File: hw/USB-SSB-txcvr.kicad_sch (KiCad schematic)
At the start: 0 parts

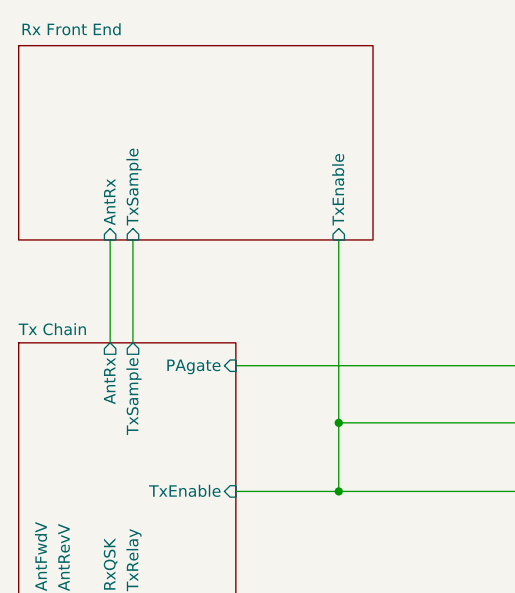
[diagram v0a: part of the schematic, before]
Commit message: Starting to move to 200 ohm share domain with tx and rx with better cheaper faster switching for attenuators and maybe QSK
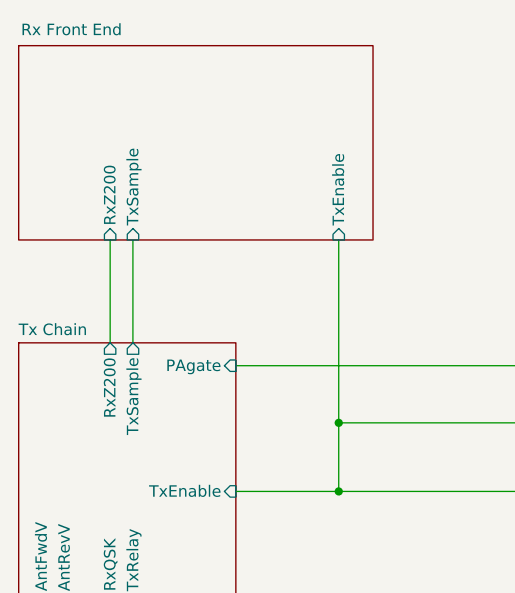
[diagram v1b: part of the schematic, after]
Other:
- sheet Rx Front End ports: added RxZ200; removed AntRx
- sheet Tx Chain ports: added RxZ200; removed AntRx
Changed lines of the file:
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@@
 			)
 		)
-		(pin "AntRx" input
+		(pin "RxZ200" input
 			(at 87.63 64.77 270)
 			(effects
@@
 			)
 		)
-		(pin "AntRx" output
+		(pin "RxZ200" output
 			(at 87.63 76.2 90)
 			(effects

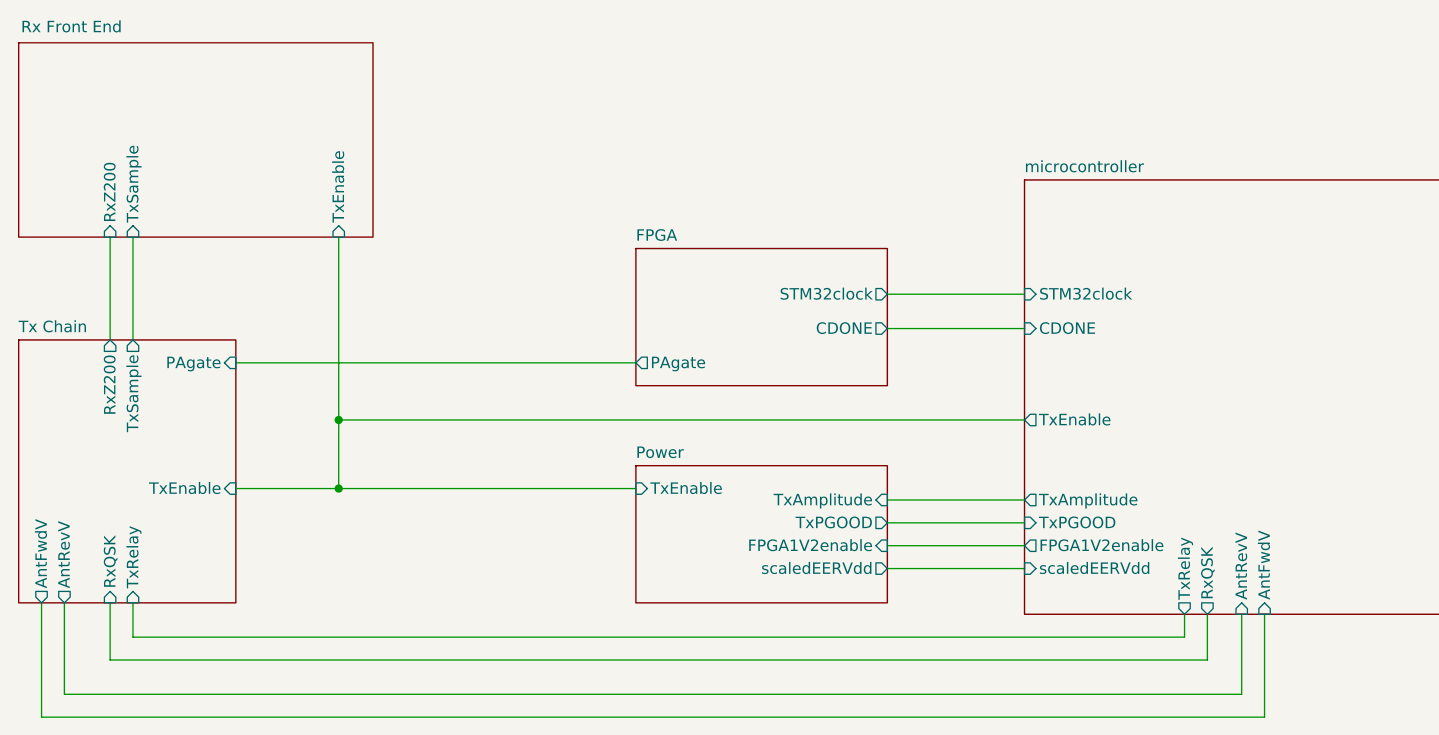
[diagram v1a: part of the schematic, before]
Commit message: Tx Veer changed to 60V max and reviewed. STM32 now provides Bruene sampling signal to control muxes for QSDs0/1 for fwd/rev complex impedance for tuner and VSWR calculation. Preselector now uses pHEMT switches, as does digital attenuator pad in rx path. Tx/rx relay is now in 200 ohm domain and rx shares most of that with tx for good selectivity and to get benefit of antenna tuner.
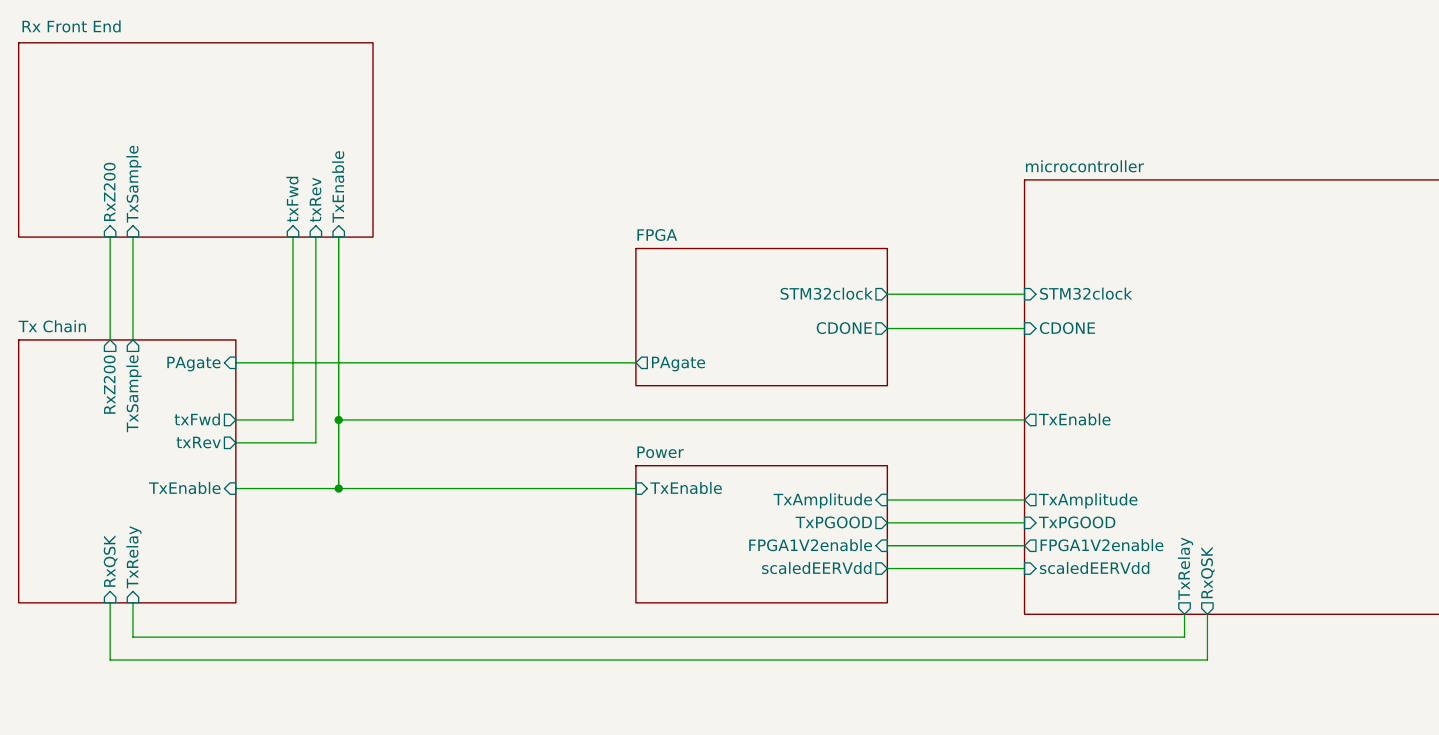
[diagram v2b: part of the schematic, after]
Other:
- sheet Rx Front End ports: added txFwd, txRev; removed none
- sheet Tx Chain ports: added txFwd, txRev; removed AntFwdV, AntRevV
- sheet microcontroller ports: added none; removed AntFwdV, AntRevV
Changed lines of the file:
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@@
 			"qsdSCK" "qsdMOSI" "tuneSCK" "tuneNSS" "tuneMOSI" "tuneMISO" "enable5V"
 			"tmpSCL" "tmpSDA" "qsdPh0a" "qsdPh0b" "qsdPh0c" "qsdPh0d" "qsdPh1a" "qsdPh1b"
-			"qsdPh1c" "qsdPh1d" "qsdPh2a" "qsdPh2b" "qsdPh2c" "qsdPh2d"
+			"qsdPh1c" "qsdPh1d" "qsdPh2a" "qsdPh2b" "qsdPh2c" "qsdPh2d" "bruene"
 		)
 	)
@@
 	(wire
 		(pts
+			(xy 110.49 87.63) (xy 101.6 87.63)
+		)
+		(stroke
+			(width 0)
+			(type default)
+		)
+	)
+	(wire
+		(pts
 			(xy 101.6 92.71) (xy 113.03 92.71)
 		)
@@
 	(wire
 		(pts
-			(xy 80.01 118.11) (xy 215.9 118.11)
-		)
-		(stroke
-			(width 0)
-			(type default)
-		)
-	)
-	(wire
-		(pts
-			(xy 80.01 105.41) (xy 80.01 118.11)
+			(xy 107.95 85.09) (xy 107.95 64.77)
 		)
 		(stroke
@@
 	(wire
 		(pts
-			(xy 82.55 115.57) (xy 82.55 105.41)
-		)
-		(stroke
-			(width 0)
-			(type default)
-		)
-	)
-	(wire
-		(pts
-			(xy 213.36 106.68) (xy 213.36 115.57)
-		)
-		(stroke
-			(width 0)
-			(type default)
-		)
-	)
-	(wire
-		(pts
 			(xy 113.03 64.77) (xy 113.03 85.09)
 		)
@@
 	(wire
 		(pts
-			(xy 213.36 115.57) (xy 82.55 115.57)
+			(xy 110.49 64.77) (xy 110.49 87.63)
 		)
 		(stroke
@@
 	(wire
 		(pts
-			(xy 215.9 118.11) (xy 215.9 106.68)
-		)
-		(stroke
-			(width 0)
-			(type default)
-		)
-	)
-	(wire
-		(pts
 			(xy 207.01 109.22) (xy 90.17 109.22)
 		)
@@
 		(pts
 			(xy 87.63 111.76) (xy 209.55 111.76)
+		)
+		(stroke
+			(width 0)
+			(type default)
+		)
+	)
+	(wire
+		(pts
+			(xy 101.6 85.09) (xy 107.95 85.09)
 		)
 		(stroke
@@
 		(pin "RxZ200" input
 			(at 87.63 64.77 270)
+			(effects
+				(font
+					(size 1.27 1.27)
+				)
+				(justify left)
+			)
+		)
+		(pin "txFwd" input
+			(at 107.95 64.77 270)
+			(effects
+				(font
+					(size 1.27 1.27)
+				)
+				(justify left)
+			)
+		)
+		(pin "txRev" input
+			(at 110.49 64.77 270)
 			(effects
 				(font
@@
 			)
 		)
-		(pin "AntFwdV" output
-			(at 80.01 105.41 270)
-			(effects
-				(font
-					(size 1.27 1.27)
-				)
-				(justify left)
-			)
-		)
-		(pin "AntRevV" output
-			(at 82.55 105.41 270)
-			(effects
-				(font
-					(size 1.27 1.27)
-				)
-				(justify left)
-			)
-		)
 		(pin "RxZ200" output
 			(at 87.63 76.2 90)
@@
 				)
 				(justify left)
+			)
+		)
+		(pin "txFwd" output
+			(at 101.6 85.09 0)
+			(effects
+				(font
+					(size 1.27 1.27)
+				)
+				(justify right)
+			)
+		)
+		(pin "txRev" output
+			(at 101.6 87.63 0)
+			(effects
+				(font
+					(size 1.27 1.27)
+				)
+				(justify right)
 			)
 		)
@@
 			(effects
 				(font
-					(size 1.27 1.27)
-				)
-				(justify left)
-			)
-		)
-		(pin "AntFwdV" input
-			(at 215.9 106.68 270)
-			(effects
-				(font
-					(size 1.27 1.27)
-				)
-				(justify left)
-			)
-		)
-		(pin "AntRevV" input
-			(at 213.36 106.68 270)
-			(effects
-				(font

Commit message: Ready for first schematic review with Claude.ai
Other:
- title: Top Level -> NexRig
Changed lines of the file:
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@@
 	(paper "USLetter")
 	(title_block
-		(title "Top Level")
+		(title "NexRig")
 		(date "2025-08-10")
 		(company "WB7NAB")
@@
 	(bus_alias "Ctrl"
 		(members "audioReset" "qsdBCLK" "qsdMCLK" "qsdWCLK" "qsdData" "qsdNSS"
-			"qsdSCK" "qsdMOSI" "tuneSCK" "tuneNSS" "tuneMOSI" "tuneMISO" "enable5V"
-			"tmpSCL" "tmpSDA" "qsdPh0a" "qsdPh0b" "qsdPh0c" "qsdPh0d" "qsdPh1a" "qsdPh1b"
-			"qsdPh1c" "qsdPh1d" "qsdPh2a" "qsdPh2b" "qsdPh2c" "qsdPh2d" "bruene" "txData"
-			"txBCLK" "txMCLK" "txWCLK" "usbReset" "usbPOK2" "usbPOK3" "usbnALERT"
-			"enable6V" "enFPGASPIVdd" "enFPGAVpp"
+			"qsdSCK" "qsdMOSI" "switchSCK" "switchMOSI" "switchRCK" "enable5V" "tmpSCL"
+			"tmpSDA" "qsdPh0a" "qsdPh0b" "qsdPh0c" "qsdPh0d" "qsdPh1a" "qsdPh1b" "qsdPh1c"
+			"qsdPh1d" "qsdPh2a" "qsdPh2b" "qsdPh2c" "qsdPh2d" "bruene" "txData" "txBCLK"
+			"txMCLK" "txWCLK" "usbReset" "usbPOK2" "usbPOK3" "usbnALERT" "enable6V"
+			"enFPGASPIVdd" "enFPGAVpp"
 		)
 	)

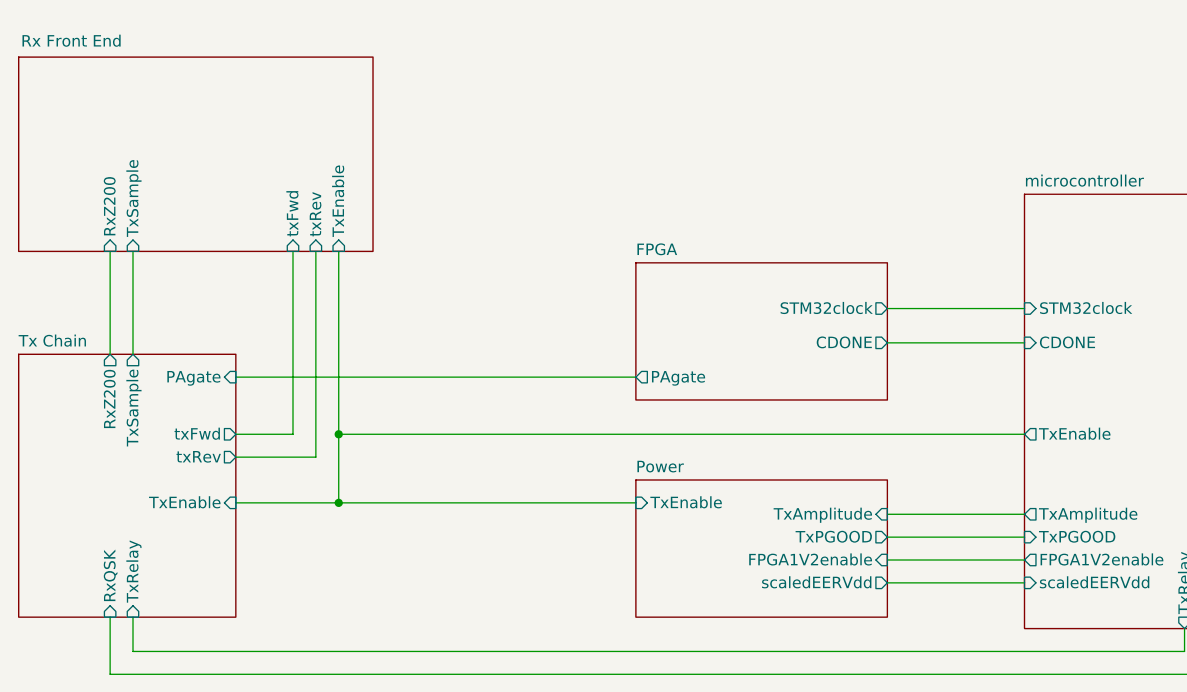
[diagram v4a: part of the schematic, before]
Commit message: Now using H bridge for differential QSE based I/Q tx
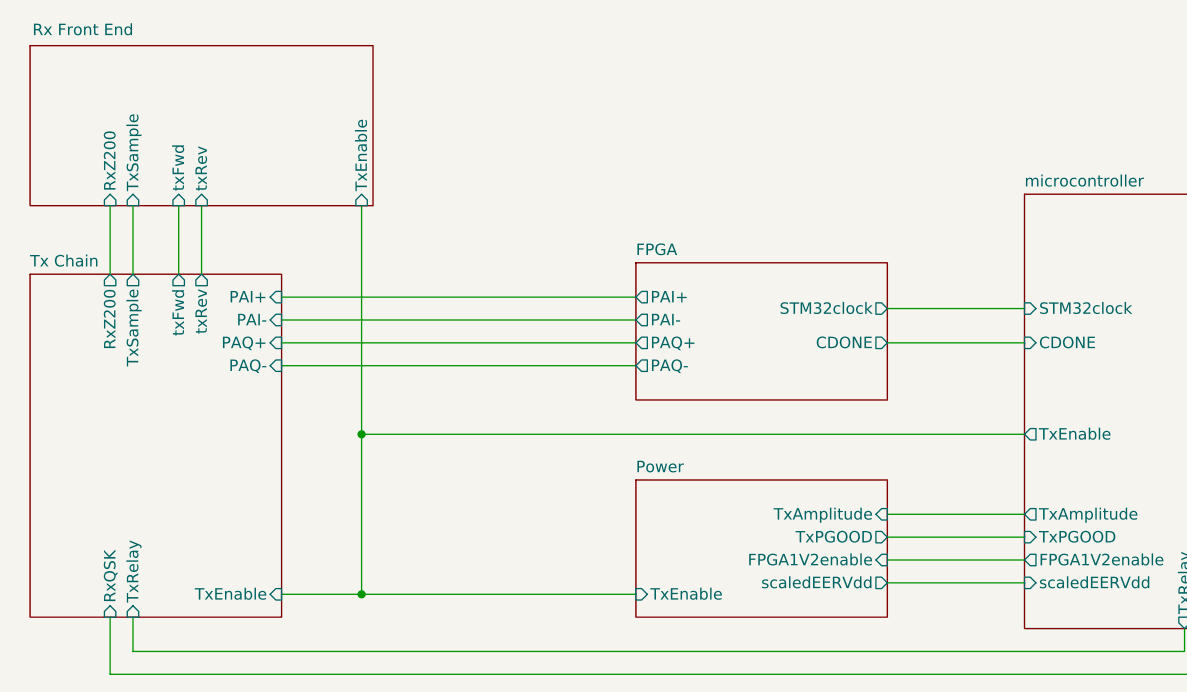
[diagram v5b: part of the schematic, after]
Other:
- sheet FPGA ports: added PAI+, PAI-, PAQ+, PAQ-; removed PAgate
- sheet Tx Chain ports: added PAI+, PAI-, PAQ+, PAQ-; removed PAgate
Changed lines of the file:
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@@
 	)
 	(junction
-		(at 113.03 92.71)
+		(at 115.57 102.87)
 		(diameter 0)
 		(color 0 0 0 0)
 	)
 	(junction
-		(at 113.03 85.09)
+		(at 115.57 85.09)
 		(diameter 0)
 		(color 0 0 0 0)
@@
 	(wire
 		(pts
+			(xy 106.68 72.39) (xy 146.05 72.39)
+		)
+		(stroke
+			(width 0)
+			(type default)
+		)
+	)
+	(wire
+		(pts
 			(xy 87.63 105.41) (xy 87.63 111.76)
 		)
@@
 	(wire
 		(pts
-			(xy 110.49 87.63) (xy 101.6 87.63)
-		)
-		(stroke
-			(width 0)
-			(type default)
-		)
-	)
-	(wire
-		(pts
-			(xy 101.6 92.71) (xy 113.03 92.71)
-		)
-		(stroke
-			(width 0)
-			(type default)
-		)
-	)
-	(wire
-		(pts
-			(xy 113.03 85.09) (xy 113.03 92.71)
-		)
-		(stroke
-			(width 0)
-			(type default)
-		)
-	)
-	(wire
-		(pts
-			(xy 113.03 85.09) (xy 189.23 85.09)
+			(xy 115.57 85.09) (xy 115.57 102.87)
+		)
+		(stroke
+			(width 0)
+			(type default)
+		)
+	)
+	(wire
+		(pts
+			(xy 106.68 102.87) (xy 115.57 102.87)
 		)
 		(stroke
@@
 	(wire
 		(pts
-			(xy 107.95 85.09) (xy 107.95 64.77)
-		)
-		(stroke
-			(width 0)
-			(type default)
-		)
-	)
-	(wire
-		(pts
-			(xy 87.63 64.77) (xy 87.63 76.2)
-		)
-		(stroke
-			(width 0)
-			(type default)
-		)
-	)
-	(wire
-		(pts
-			(xy 113.03 64.77) (xy 113.03 85.09)
+			(xy 115.57 102.87) (xy 146.05 102.87)
+		)
+		(stroke
+			(width 0)
+			(type default)
+		)
+	)
+	(wire
+		(pts
+			(xy 115.57 59.69) (xy 115.57 85.09)
+		)
+		(stroke
+			(width 0)
+			(type default)
+		)
+	)
+	(wire
+		(pts
+			(xy 106.68 69.85) (xy 146.05 69.85)
+		)
+		(stroke
+			(width 0)
+			(type default)
+		)
+	)
+	(wire
+		(pts
+			(xy 115.57 85.09) (xy 189.23 85.09)
+		)
+		(stroke
+			(width 0)
+			(type default)
+		)
+	)
+	(wire
+		(pts
+			(xy 95.25 67.31) (xy 95.25 59.69)
+		)
+		(stroke
+			(width 0)
+			(type default)
+		)
+	)
+	(wire
+		(pts
+			(xy 90.17 59.69) (xy 90.17 67.31)
 		)
 		(stroke
@@
 	(wire
 		(pts
+			(xy 106.68 77.47) (xy 146.05 77.47)
+		)
+		(stroke
+			(width 0)
+			(type default)
+		)
+	)
+	(wire
+		(pts
+			(xy 106.68 74.93) (xy 146.05 74.93)
+		)
+		(stroke
+			(width 0)
+			(type default)
+		)
+	)
+	(wire
+		(pts
 			(xy 173.99 93.98) (xy 189.23 93.98)
 		)
@@
 	(wire
 		(pts
-			(xy 110.49 64.77) (xy 110.49 87.63)
-		)
-		(stroke
-			(width 0)
-			(type default)
-		)
-	)
-	(wire
-		(pts
-			(xy 113.03 92.71) (xy 146.05 92.71)
+			(xy 97.79 59.69) (xy 97.79 67.31)
 		)
 		(stroke
@@
 	(wire
 		(pts
-			(xy 101.6 85.09) (xy 107.95 85.09)
-		)
-		(stroke
-			(width 0)
-			(type default)
-		)
-	)
-	(wire
-		(pts
-			(xy 101.6 78.74) (xy 146.05 78.74)
+			(xy 87.63 59.69) (xy 87.63 67.31)
 		)
 		(stroke
@@
 	(wire
 		(pts
-			(xy 90.17 64.77) (xy 90.17 76.2)
-		)
-		(stroke
-			(width 0)
-			(type default)
-		)
-	)
-	(wire
-		(pts
 			(xy 209.55 111.76) (xy 209.55 106.68)
 		)
@@
 	)
 	(sheet
-		(at 77.47 43.18)
-		(size 39.37 21.59)
+		(at 78.74 41.91)
+		(size 38.1 17.78)
 		(exclude_from_sim no)
 		(in_bom yes)
@@
 		)
 		(property "Sheetname" "Rx Front End"
-			(at 77.724 42.164 0)
+			(at 78.994 40.894 0)
 			(effects
 				(font
@@
 		)
 		(property "Sheetfile" "rx-signal-chain.kicad_sch"
-			(at 112.0906 64.77 90)
+			(at 113.3606 63.5 90)
 			(effects
 				(font
@@
 		)
 		(pin "TxSample" input
-			(at 90.17 64.77 270)
+			(at 90.17 59.69 270)
 			(effects
 				(font
@@
 		)
 		(pin "TxEnable" input
-			(at 113.03 64.77 270)
+			(at 115.57 59.69 270)
 			(effects
 				(font
@@
 		)
 		(pin "RxZ200" input
-			(at 87.63 64.77 270)
+			(at 87.63 59.69 270)
 			(effects
 				(font
@@
 		)
 		(pin "txFwd" input
-			(at 107.95 64.77 270)
+			(at 95.25 59.69 270)
 			(effects
 				(font
@@
 		)
 		(pin "txRev" input
-			(at 110.49 64.77 270)
+			(at 97.79 59.69 270)
 			(effects
 				(font
@@
 			)
 		)
-		(pin "PAgate" output
-			(at 146.05 78.74 180)
-			(effects
-				(font
-					(size 1.27 1.27)
-				)
-				(justify left)
-			)
-		)
 		(pin "STM32clock" output
 			(at 173.99 71.12 0)
@@
 				)
 				(justify right)
+			)
+		)
+		(pin "PAI+" output
+			(at 146.05 69.85 180)
+			(effects
+				(font
+					(size 1.27 1.27)
+				)
+				(justify left)
+			)
+		)
+		(pin "PAI-" output
+			(at 146.05 72.39 180)
+			(effects
+				(font
+					(size 1.27 1.27)
+				)
+				(justify left)
+			)
+		)
+		(pin "PAQ+" output
+			(at 146.05 74.93 180)
+			(effects
+				(font
+					(size 1.27 1.27)
+				)
+				(justify left)
+			)
+		)
+		(pin "PAQ-" output
+			(at 146.05 77.47 180)
+			(effects
+				(font
+					(size 1.27 1.27)
+				)
+				(justify left)
 			)
 		)
@@
 	)
 	(sheet
-		(at 77.47 76.2)
-		(size 24.13 29.21)
+		(at 78.74 67.31)
+		(size 27.94 38.1)
 		(exclude_from_sim no)
 		(in_bom yes)
@@
 		)
 		(property "Sheetname" "Tx Chain"
-			(at 77.47 75.4884 0)
+			(at 78.74 66.5984 0)
 			(effects
 				(font
@@
 		)
 		(property "Sheetfile" "tx-signal-chain.kicad_sch"
-			(at 77.47 105.9946 0)
+			(at 78.74 105.9946 0)
 			(effects
 				(font
@@
 		)
 		(pin "TxSample" output
-			(at 90.17 76.2 90)
+			(at 90.17 67.31 90)
 			(effects
 				(font
@@
 		)
 		(pin "TxEnable" input
-			(at 101.6 92.71 0)
-			(effects
-				(font
-					(size 1.27 1.27)
-				)
-				(justify right)
-			)
-		)
-		(pin "PAgate" input
-			(at 101.6 78.74 0)
+			(at 106.68 102.87 0)
 			(effects
 				(font
@@
 		)
 		(pin "RxZ200" output
-			(at 87.63 76.2 90)
+			(at 87.63 67.31 90)
 			(effects
 				(font
@@
 		)
 		(pin "txFwd" output
-			(at 101.6 85.09 0)
+			(at 95.25 67.31 90)
 			(effects
 				(font
@@
 		)
 		(pin "txRev" output
-			(at 101.6 87.63 0)
+			(at 97.79 67.31 90)
+			(effects
+				(font
+					(size 1.27 1.27)
+				)
+				(justify right)
+			)
+		)
+		(pin "PAI+" input
+			(at 106.68 69.85 0)
+			(effects
+				(font
+					(size 1.27 1.27)
+				)
+				(justify right)
+			)
+		)
+		(pin "PAI-" input
+			(at 106.68 72.39 0)
+			(effects
+				(font
+					(size 1.27 1.27)
+				)
+				(justify right)
+			)
+		)
+		(pin "PAQ+" input
+			(at 106.68 74.93 0)
+			(effects
+				(font
+					(size 1.27 1.27)
+				)
+				(justify right)
+			)
+		)
+		(pin "PAQ-" input
+			(at 106.68 77.47 0)
 			(effects
 				(font
@@
 		)
 		(pin "TxEnable" input
-			(at 146.05 92.71 180)
-			(effects
-				(font
+			(at 146.05 102.87 180)
+			(effects
+				(font
